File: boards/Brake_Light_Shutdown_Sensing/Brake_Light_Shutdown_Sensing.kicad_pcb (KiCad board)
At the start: 2 copper layers, 70 x 70 mm, 85 parts, among them IC1 ATMEGA16M1, J1 micromatch_female_RA_10, J2 micromatch_female_RA_20, P1 CONN_02X03, Q1 SSM3K333R, Q2 SSM3K333R, Q3 SSM3K333R, Q4 SSM3K333R, Q5 SSM3K333R, Q6 SSM3K333R, Q7 SSM3K333R, U1 MCP6001RT, U2 TPS561201, U3 CP2120, U4 LM1117-1.8, U5 CAN_Transceiver, Y1 Crystal_SMD

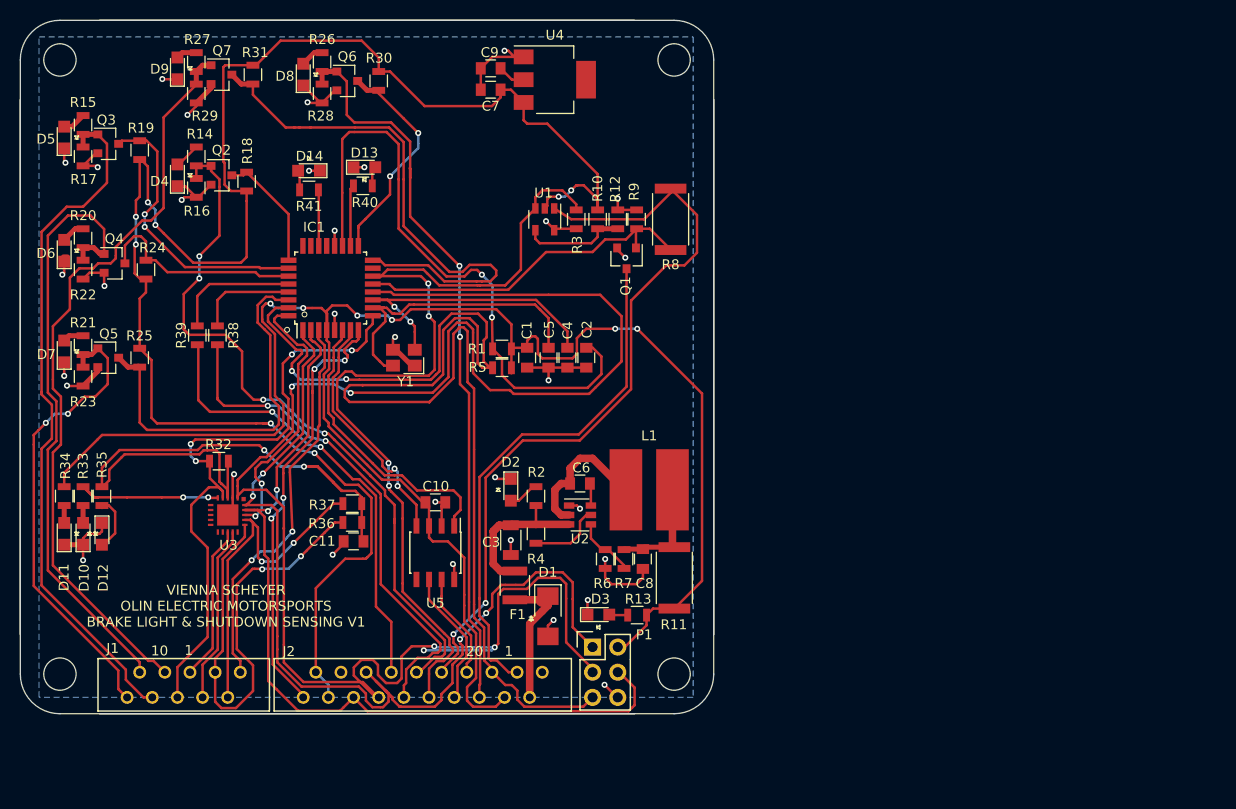
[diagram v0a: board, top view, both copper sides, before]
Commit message: Starting new pcb layout with updated schematic (Atmega 16)
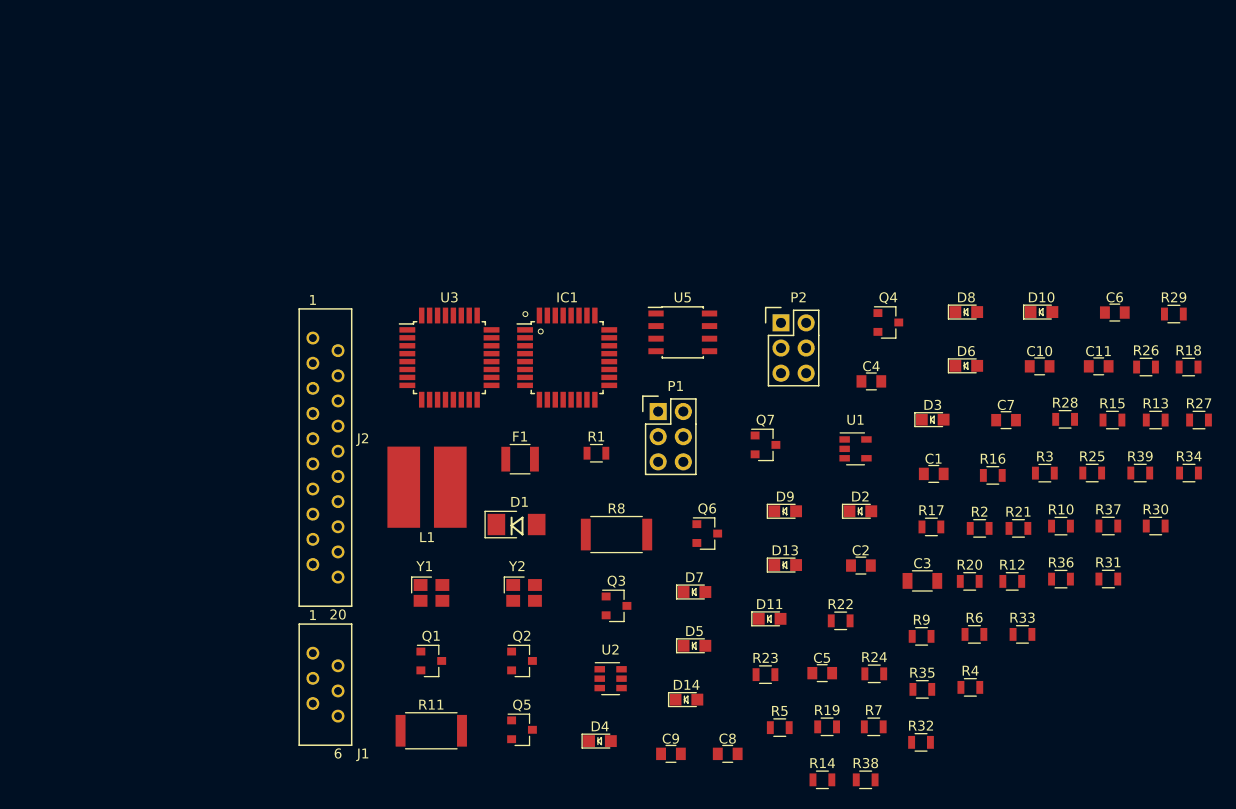
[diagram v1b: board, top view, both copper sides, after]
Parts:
- removed D12: LED_0805, footprints:LED_0805_OEM
- removed R40, R41: R_1k, footprints:R_0805_OEM
- removed U4: LM1117-1.8, TO_SOT_Packages_SMD:SOT-223
- added P2: CONN_02X03, footprints:Pin_Header_Straight_2x03, F.Cu at (190.3, 100.5)
- added Y2: Crystal_SMD, footprints:Crystal_SMD_FA238, F.Cu at (164.4, 127.8)
- C11, C9: value C_0.1uF -> C_30pF
- J1: value micromatch_female_RA_10 -> micromatch_female_RA_6; footprint footprints:micromatch_female_ra_10 -> footprints:micromatch_female_ra_6
- R32: value 4.7K -> R_200
- R33, R34, R35: value R_1k -> R_200
- R36, R37: value 4.7K -> R_10k
- U3: value CP2120 -> ATMEGA328P-AU; footprint footprints:CP2120-QFN -> Housings_QFP:TQFP-32_7x7mm_Pitch0.8mm
- moved R34 113.6 mm to (231.5, 115.7), turned to 0 degrees
- moved R15 108.1 mm to (223.8, 110.4), turned to 0 degrees
- moved R27 107.5 mm to (232.5, 110.4), turned to 0 degrees
- moved R29 101.2 mm to (230.0, 99.7), turned to 0 degrees
- moved R31 100.2 mm to (223.3, 126.4), turned to 0 degrees
- moved D10 99.3 mm to (216.6, 99.5), turned to 0 degrees
- moved R18 96.9 mm to (231.4, 105.0), turned to 0 degrees
- moved R25 96.9 mm to (221.7, 115.7), turned to 0 degrees
- moved R21 96.2 mm to (214.3, 121.3), turned to 0 degrees
- moved R20 96.0 mm to (209.3, 126.6), turned to 0 degrees
- moved R33 95.9 mm to (214.7, 132.0), turned to 0 degrees
- moved R39 94.2 mm to (226.6, 115.7), turned to 0 degrees
- moved R17 93.4 mm to (205.5, 121.1), turned to 0 degrees
- moved D6 91.8 mm to (209.0, 104.9), turned to 0 degrees
- moved R19 90.6 mm to (194.9, 141.3), turned to 0 degrees
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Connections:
- C11 pad 1: +3V3 -> /XTAL1
- C7 pad 1: +5V -> VCC
- C9 pad 1: /3.3V -> /XTAL2
- IC1 pad 14: /Brake_Switch- -> /data2
- IC1 pad 15: Net-(IC1-Pad15) -> /data1
- IC1 pad 23: Net-(IC1-Pad23) -> /BSPD_Out
- IC1 pad 24: Net-(IC1-Pad24) -> /data4
- IC1 pad 32: /CS -> /data3
- IC1 pad 9: /RST -> /RESET
- J1 pad 1: /BSPD_Sense -> /Main_Sense
- J1 pad 2: /R_E-Stop_Sense -> /L_E-Stop_Sense
- J1 pad 3: /TSMS_Sense -> /R_E-Stop_Sense
- J1 pad 4: /HVD_Sense -> /BSPD_Sense
- J1 pad 5: /RST -> /HVD_Sense
- J1 pad 6: /EINT -> /TSMS_Sense
- J2 pad 10: /Brake_Switch- -> /LED_1
- J2 pad 11: /Main_Sense -> /LED_2
- J2 pad 12: /LED_2 -> /Brake_Light_LSD
- J2 pad 13: /LED_1 -> +5V
- J2 pad 14: /SCK -> /Brake_Switch-
- J2 pad 15: /MISO -> /BSPD_Out
- J2 pad 16: /MOSI -> /BSPD_Stat_Out
- J2 pad 17: GND -> /SDA
- J2 pad 18: +5V -> /SCL
- J2 pad 19: +5V -> /Analog_Brake_Sense
- J2 pad 20: /Analog_Brake_Sense -> Net-(J2-Pad20)
- J2 pad 3: /Brake_Light_LSD -> VCC
- J2 pad 4: VCC -> /MOSI
- J2 pad 5: /RESET -> /MISO
- J2 pad 6: /L_E-Stop_Sense -> /SCK
- J2 pad 7: /CAN_high -> /RESET
- J2 pad 8: /CAN_low -> /CAN_high
- J2 pad 9: /BSPD_Out -> /CAN_low
- R32 pad 1: +3V3 -> /LED_3
- R32 pad 2: /RST -> Net-(D13-Pad2)
- R33 pad 1: /GPIO_O -> /LED_4
- R33 pad 2: Net-(D10-Pad2) -> Net-(D14-Pad2)
- R34 pad 1: VCC -> /LED5
- R34 pad 2: Net-(D11-Pad2) -> Net-(D10-Pad2)
- R35 pad 1: +3V3 -> /LED6
- R35 pad 2: Net-(D12-Pad2) -> Net-(D11-Pad2)
- R36 pad 1: +3V3 -> VCC
- R36 pad 2: /SCL -> /RST32
- R37 pad 1: +3V3 -> VCC
- R37 pad 2: /SDA -> /data1
- U3 pad 1: /SCK -> Net-(U3-Pad1)
- U3 pad 11: Net-(U3-Pad11) -> /data4
- U3 pad 12: Net-(U3-Pad12) -> /data3
- U3 pad 13: /EINT -> /data2
- U3 pad 14: /INT -> /data1
- U3 pad 15: Net-(U3-Pad15) -> /MOSI
- U3 pad 16: /SCL -> /MISO
- U3 pad 17: /SDA -> /SCK
- U3 pad 18: /CS -> VCC
- U3 pad 19: /MOSI -> Net-(U3-Pad19)
- U3 pad 2: GND -> Net-(U3-Pad2)
- U3 pad 20: /MISO -> VCC
- U3 pad 3: +3V3 -> GND
- U3 pad 4: /RST -> VCC
- U3 pad 5: /GPIO_O -> GND
- U3 pad 6: Net-(U3-Pad6) -> VCC
- U3 pad 7: Net-(U3-Pad7) -> /XTAL1
- U3 pad 8: Net-(U3-Pad8) -> /XTAL2
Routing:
- net VCC: track 186.6 -> 0.00 mm, vias 6 -> 0
- net +5V: track 178.7 -> 0.00 mm, vias 8 -> 0
- net /SCK: track 177.4 -> 0.00 mm, vias 5 -> 0
- net /RESET: track 135.1 -> 0.00 mm, vias 2 -> 0
- net GND: track 105.6 -> 0.00 mm, vias 32 -> 0
- net /MISO: track 96.9 -> 0.00 mm, vias 4 -> 0
- net /Brake_Switch-: track 94.2 -> 0.00 mm, vias 4 -> 0
- net /MOSI: track 86.2 -> 0.00 mm, vias 2 -> 0
- net /BSPD_Out: track 79.5 -> 0.00 mm, vias 2 -> 0
- net /HVD_Sense: track 76.4 -> 0.00 mm
- net /L_E-Stop_Sense: track 75.5 -> 0.00 mm, vias 2 -> 0
- net /Main_Sense: track 73.2 -> 0.00 mm, vias 4 -> 0
- net /TSMS_Sense: track 69.8 -> 0.00 mm
- net +3V3: track 63.1 -> 0.00 mm, vias 2 -> 0
- net Net-(C2-Pad1): track 62.6 -> 0.00 mm, vias 2 -> 0
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- removed copper zone on B.Cu, net GND
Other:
- board outline removed
- board text removed: "VIENNA SCHEYER OLIN ELECTRIC MOTORSPORTS BRAKE LIGHT & SHUTDOWN SENSING V1"

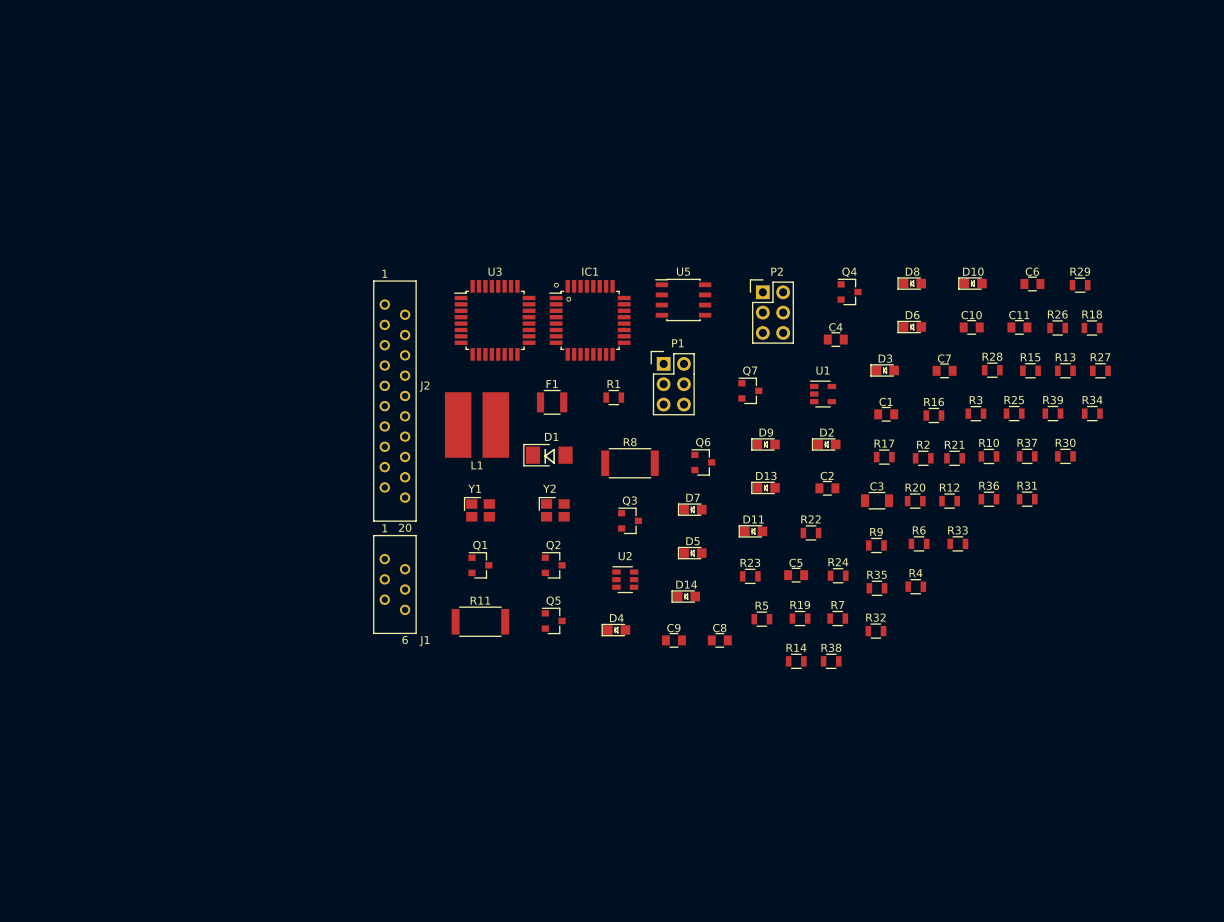
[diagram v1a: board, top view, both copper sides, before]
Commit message: Started layout
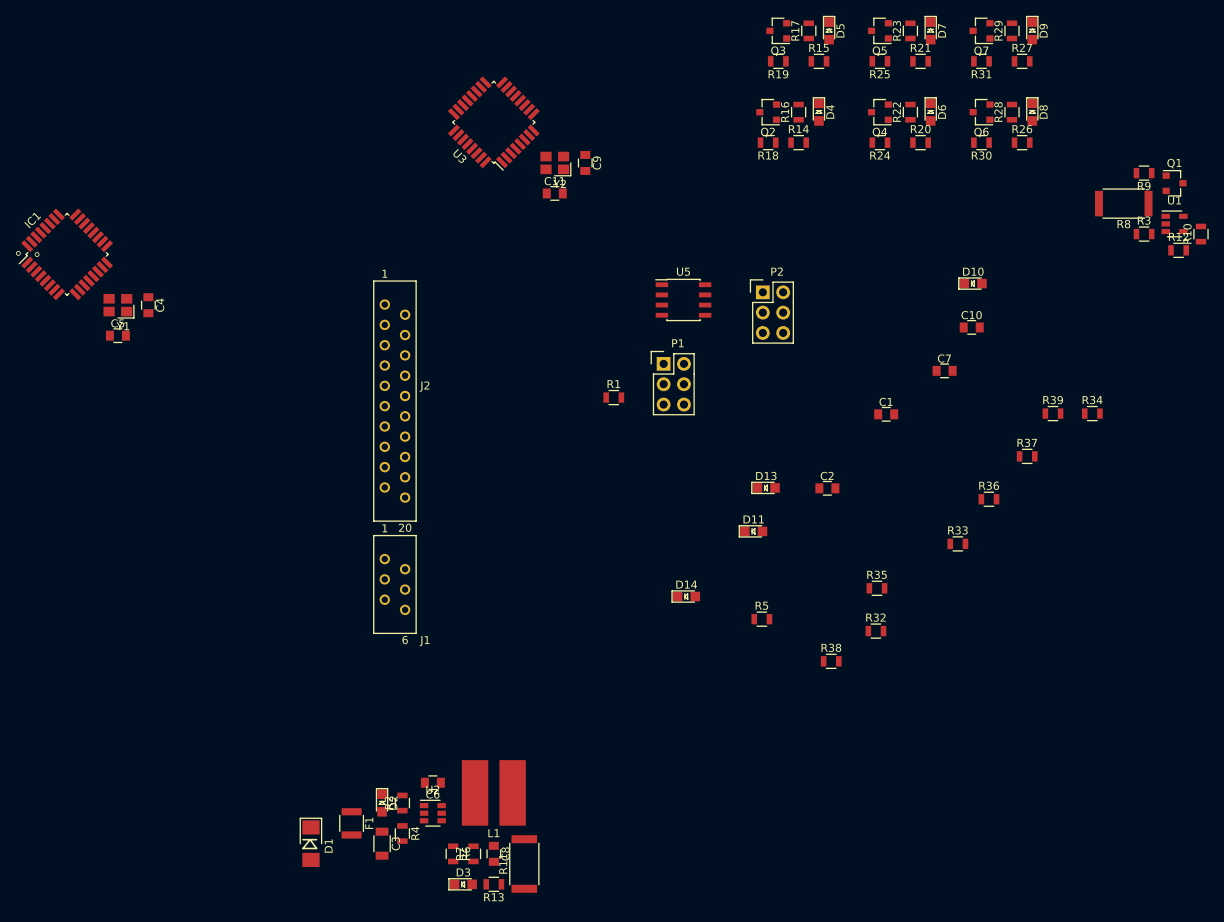
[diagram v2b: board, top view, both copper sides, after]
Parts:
- moved Q1 99.0 mm to (241.8, 86.9)
- moved C6 97.5 mm to (149.0, 161.8), turned to 180 degrees
- moved R13 96.1 mm to (156.7, 174.5), turned to 180 degrees
- moved C5 89.9 mm to (109.7, 106.0)
- moved C4 86.0 mm to (113.5, 102.2), turned to 270 degrees
- moved Q5 84.3 mm to (204.9, 67.9), turned to 180 degrees
- moved D3 83.1 mm to (152.9, 174.5)
- moved R2 78.1 mm to (145.2, 164.4), turned to 90 degrees
- moved C3 75.3 mm to (142.7, 169.5), turned to 270 degrees
- moved D2 71.4 mm to (142.7, 164.4), turned to 270 degrees
- moved R4 71.2 mm to (145.2, 168.2), turned to 270 degrees
- moved R23 71.1 mm to (208.7, 67.9), turned to 90 degrees
- moved R6 69.9 mm to (151.6, 170.7), turned to 270 degrees
- moved R8 69.7 mm to (235.4, 89.5), turned to 180 degrees
- moved R19 69.7 mm to (192.2, 71.7), turned to 180 degrees
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
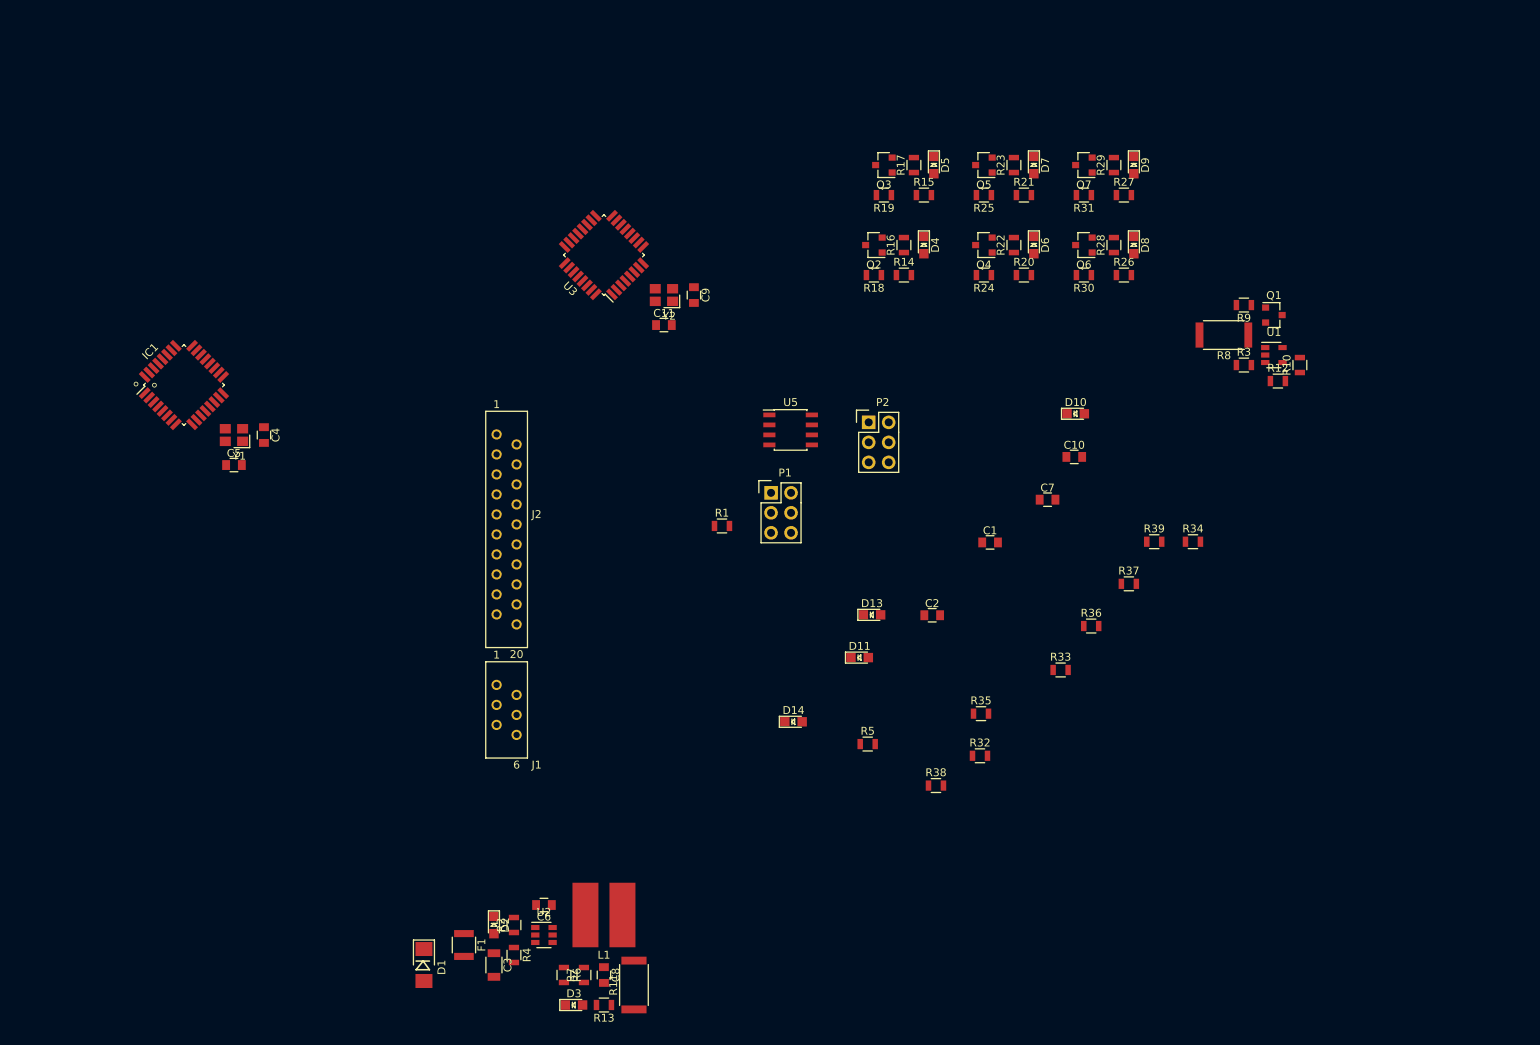
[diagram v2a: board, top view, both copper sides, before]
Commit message: Updated Layout (added bypass cap to Brake Light Circuit), continued with layout, and started tracing modules
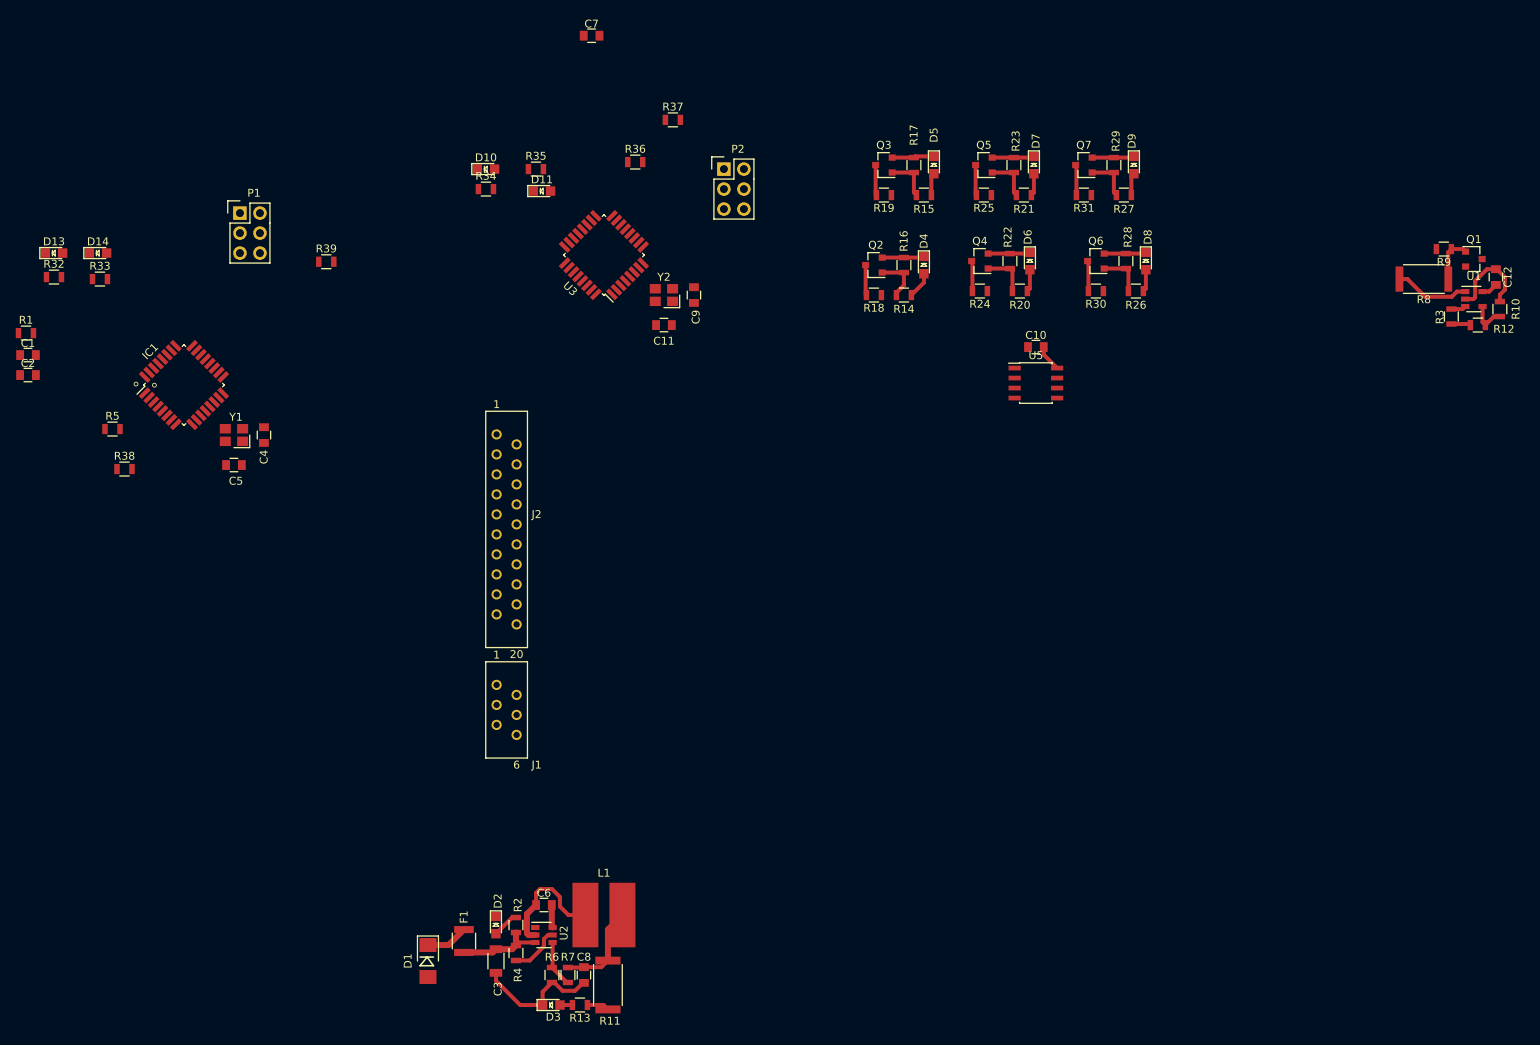
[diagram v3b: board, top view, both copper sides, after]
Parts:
- added C12: C_0.1uF, footprints:C_0805_OEM, F.Cu at (270.0, 82.1)
- moved R32 132.4 mm to (86.8, 82.1)
- moved R33 131.7 mm to (92.7, 82.3)
- moved C1 124.5 mm to (83.5, 92.0)
- moved C2 118.8 mm to (83.5, 94.5)
- moved D13 113.6 mm to (86.8, 79.0)
- moved R39 111.0 mm to (121.4, 80.1)
- moved R38 110.6 mm to (95.8, 106.5)
- moved D14 106.5 mm to (92.4, 79.0)
- moved R5 103.9 mm to (94.2, 101.4)
- moved R34 100.3 mm to (141.7, 70.9)
- moved R1 91.7 mm to (83.3, 89.2)
- moved R35 89.3 mm to (148.0, 68.4)
- moved R36 82.6 mm to (160.6, 67.5)
- moved R37 82.6 mm to (165.4, 62.1)
- moved C7 82.6 mm to (155.1, 51.4)
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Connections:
- P2 pad 1: /MISO -> /32
- P2 pad 3: /SCK -> /SCK32
- P2 pad 4: /MOSI -> /MOSI32
- U3 pad 15: /MOSI -> /MOSI32
- U3 pad 16: /MISO -> /MISO32
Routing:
- net GND: track 0.00 -> 56.5 mm
- net Net-(C6-Pad2): track 0.00 -> 15.3 mm
- net Net-(C8-Pad1): track 0.00 -> 12.0 mm
- net +5V: track 0.00 -> 11.6 mm
- net Net-(C3-Pad1): track 0.00 -> 11.2 mm
- net /BSPD_Out: track 0.00 -> 9.55 mm
- net Net-(R4-Pad2): track 0.00 -> 6.54 mm
- net Net-(R6-Pad1): track 0.00 -> 6.03 mm
- net /Main_Sense: track 0.00 -> 6.01 mm
- net /Brake_Light_Gate: track 0.00 -> 5.91 mm
- net /TSMS_Sense: track 0.00 -> 5.75 mm
- net /R_E-Stop_Sense: track 0.00 -> 5.75 mm
- net /L_E-Stop_Sense: track 0.00 -> 5.75 mm
- net /HVD_Sense: track 0.00 -> 5.75 mm
- net /BSPD_Sense: track 0.00 -> 5.75 mm
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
